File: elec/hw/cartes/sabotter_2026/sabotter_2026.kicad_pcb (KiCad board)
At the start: 4 copper layers, 65 x 100 mm, 139 parts, among them J1 22272021, J10 2-1445051-3, J11 22272051, J12 22272031, J13 3-794630-6, J17 22272061, J3 USB4120-03-C, J5 22272041, J6 3-794630-4, J9 3-794630-4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

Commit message: sabotter corrected after review
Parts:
- removed the R65 at (164.6, 81.8)
- removed the SW3 at (170.0, 79.2)
- added R27: 100k, cocotter_resistor:r0603_reflow, F.Cu at (113.0, 67.2)
- added R35: 100k, cocotter_resistor:r0603_reflow, F.Cu at (113.0, 65.5)
- added R36: 100k, cocotter_resistor:r0603_reflow, F.Cu at (113.0, 63.9)
- added R37: 0R, cocotter_resistor:r0603_reflow, F.Cu at (122.0, 93.8)
- D3: value 1N5819WS -> BZT52C3V0S; footprint cocotter_diodes:D_SOD-323 -> cocotter_diodes:SOD-323
- R1: value 22k 1% -> 100k
- R13, R14, R15, R2, R21, R24, R26, R30, R31, R32, R33, R34, R40, R42, R44, R46, R49, R51, R52, R55, R62, R63, R64, R68: value 91k 1% -> 100k
- moved D3 4.10 mm to (159.2, 22.5)
- moved R1 2.70 mm to (113.0, 62.2), turned to 180 degrees
- moved R2 1.00 mm to (161.5, 25.2)
- moved C3 1.00 mm to (161.5, 22.0)
- moved R3 1.00 mm to (163.5, 22.0)
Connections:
- net /interfaces/i2C_io_int_3v3 renamed /interfaces/irq_io_3v3
- D2 pad A: Net-(D1-K) -> Net-(D2-PadA)
- D2 pad C: Net-(D2-PadC) -> GND
- D3 pad 1: +3V3 -> /uc/esp32_vbatt_mon_3v1
- D3 pad 2: /uc/esp32_vbatt_mon_3v1 -> GND
- J18 pad 3: (no net) -> Net-(J18-NC)
- R1 pad 1: Net-(D2-PadC) -> Net-(D1-K)
- R1 pad 2: GND -> Net-(D2-PadA)
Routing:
- net /motors/ENCODER_A_MOT2_3V3: track 190.4 -> 90.4 mm
- net /motors/ENCODER_B_MOT0_3V3: track 147.7 -> 90.8 mm
- net /motors/ENCODER_B_MOT1_3V3: track 39.0 -> 92.4 mm
- net /motors/ENCODER_A_MOT0_3V3: track 119.6 -> 79.6 mm
- net /motors/DIR_MOT0_3V3: track 59.4 -> 89.0 mm
- net /motors/ENCODER_B_MOT2_3V3: track 111.1 -> 88.4 mm
- net /motors/irq0_3v3: track 68.2 -> 50.5 mm
- net /brake_mot_3v3: track 79.1 -> 63.3 mm
- net /interfaces/scl_3v3: track 147.1 -> 132.8 mm
- net /motors/DIR_MOT1_3V3: track 94.7 -> 107.1 mm
- net /uc/EN_ESP32_3v3: track 84.9 -> 74.9 mm
- net /interfaces/ctc_right_3v3: track 22.7 -> 15.2 mm
- net /interfaces/ctc_left_3v3: track 30.2 -> 23.2 mm
- net Net-(D2-PadA): track 0.00 -> 6.55 mm
- net +5V: track 188.8 -> 195.3 mm, vias 16 -> 17
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
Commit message: sabotter updated after review
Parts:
- added R38: 0R, cocotter_resistor:r0603_reflow, F.Cu at (161.5, 31.0)
- added R72: 0R, cocotter_resistor:r0603_reflow, F.Cu at (166.0, 33.8)
- added R73: 0R, cocotter_resistor:r0603_reflow, F.Cu at (146.5, 43.8)
- added R74: 0R, cocotter_resistor:r0603_reflow, F.Cu at (147.9, 43.8)
- added R75: 0R, cocotter_resistor:r0603_reflow, F.Cu at (134.2, 31.5)
- added R76: 0R, cocotter_resistor:r0603_reflow, F.Cu at (134.2, 32.9)
- R16, R17: value 390R 1% -> 0R
- R30, R33: value 100k -> 0R
- moved R29 37.3 mm to (160.5, 25.5), turned to 180 degrees
- moved R28 36.6 mm to (158.5, 33.8)
- moved R30 29.6 mm to (143.7, 43.8), turned to 90 degrees
- moved R33 28.2 mm to (145.1, 43.8)
- moved R2 2.02 mm to (163.5, 25.0)
- moved R31 1.72 mm to (160.0, 31.0), turned to -90 degrees
- moved TP6 1.00 mm to (116.5, 54.8)
- moved R32 0.75 mm to (166.6, 35.8)
- moved R34 0.75 mm to (166.6, 37.2)
- moved TP1 0.65 mm to (149.9, 44.8)
- moved C7 0.30 mm to (121.5, 69.7)
- moved C6 0.20 mm to (126.5, 61.2)
- moved J3 0.20 mm to (114.8, 44.0)
- moved TP3 0.18 mm to (133.1, 30.1)
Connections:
- J5 pad 1: /sensors/lidar_rx_3v3 -> Net-(J5-Pad1)
- J5 pad 2: /sensors/lidar_pwm_3v3 -> Net-(J5-Pad2)
- R30 pad 1: +3V3 -> /motors/ENCODER_A_MOT0_3V3
- R30 pad 2: /sensors/lidar_pwm_3v3 -> Net-(U3-IO11,RTC_GPIO11,GPIO11,TOUCH11,FSPID,FSPIIO5,SUBSPID)
- R33 pad 1: +3V3 -> /motors/ENCODER_B_MOT0_3V3
- R33 pad 2: /sensors/lidar_rx_3v3 -> Net-(U3-IO12,RTC_GPIO12,GPIO12,TOUCH12,FSPICLK,FSPIIO6,SUBSPICLK)
- U3 pad 19: /motors/ENCODER_A_MOT0_3V3 -> Net-(U3-IO11,RTC_GPIO11,GPIO11,TOUCH11,FSPID,FSPIIO5,SUBSPID)
- U3 pad 20: /motors/ENCODER_B_MOT0_3V3 -> Net-(U3-IO12,RTC_GPIO12,GPIO12,TOUCH12,FSPICLK,FSPIIO6,SUBSPICLK)
- U3 pad 21: /motors/ENCODER_B_MOT2_3V3 -> Net-(U3-IO13,RTC_GPIO13,GPIO13,TOUCH13,FSPIQ,FSPIIO7,SUBSPIQ)
- U3 pad 22: /motors/ENCODER_A_MOT2_3V3 -> Net-(U3-IO14,RTC_GPIO14,GPIO14,TOUCH14,FSPIWP,FSPIDQS,SUBSPIWP)
- U3 pad 8: /motors/ENCODER_B_MOT1_3V3 -> Net-(U3-IO15,RTC_GPIO15,GPIO15,U0RTS,XTAL_32K_P)
- U3 pad 9: /motors/ENCODER_A_MOT1_3V3 -> Net-(U3-IO16,RTC_GPIO16,GPIO16,U0CTS,XTAL_32K_N)
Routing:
- net /sensors/rx_from_r3d2_3v3: track 4.81 -> 42.1 mm
- net /sensors/lidar_rx_3v3: track 50.9 -> 14.4 mm
- net /sensors/tx_to_r3d2_3v3: track 3.85 -> 40.0 mm, vias 1 -> 3
- net /sensors/lidar_pwm_3v3: track 51.0 -> 23.2 mm
- net /motors/ENCODER_B_MOT0_3V3: track 90.8 -> 76.4 mm
- net +3V3: track 88.8 -> 84.5 mm, vias 27 -> 25
- net /motors/ENCODER_A_MOT0_3V3: track 79.6 -> 75.4 mm
- net /motors/ENCODER_A_MOT1_3V3: track 91.8 -> 88.0 mm
- net /motors/ENCODER_B_MOT1_3V3: track 92.4 -> 88.6 mm
- net /motors/ENCODER_A_MOT2_3V3: track 90.4 -> 86.6 mm
- net Net-(D1-K): track 106.5 -> 109.9 mm
- net /motors/ENCODER_B_MOT2_3V3: track 88.4 -> 85.1 mm
- net Net-(U3-IO12,RTC_GPIO12,GPIO12,TOUCH12,FSPICLK,FSPIIO6,SUBSPICLK): track 0.00 -> 2.76 mm
- net Net-(U3-IO11,RTC_GPIO11,GPIO11,TOUCH11,FSPID,FSPIIO5,SUBSPID): track 0.00 -> 2.72 mm
- net Net-(J5-Pad1): track 0.00 -> 2.59 mm
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
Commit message: jlcpcb part added
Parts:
- C6, C7: value 22µF 16V -> 22µF 25V
- J14, J15, J16: value ~ -> 1-188275-6
- J18, J4: value ~ -> 188275-4
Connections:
- J4 pad 3: (no net) -> unconnected-(J4-NC-Pad3)

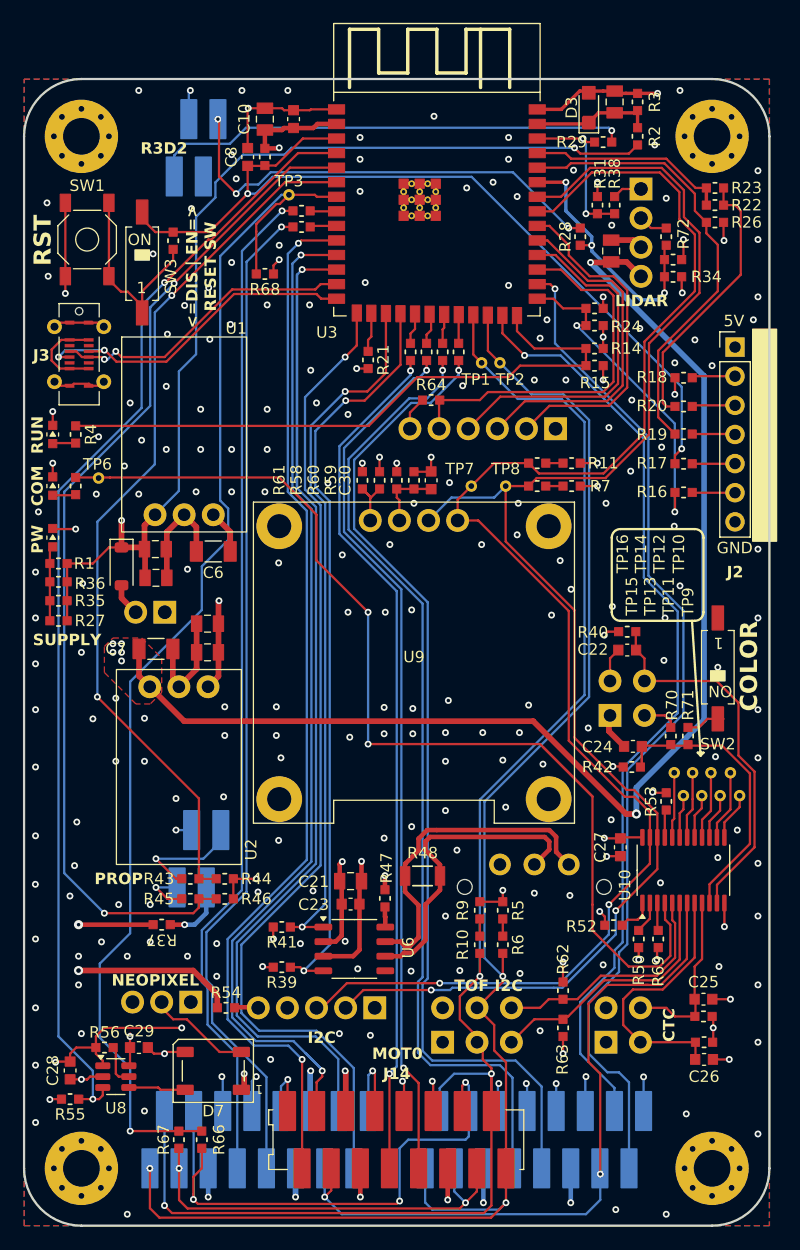
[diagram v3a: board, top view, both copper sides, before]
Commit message: oki78 footprint corrected
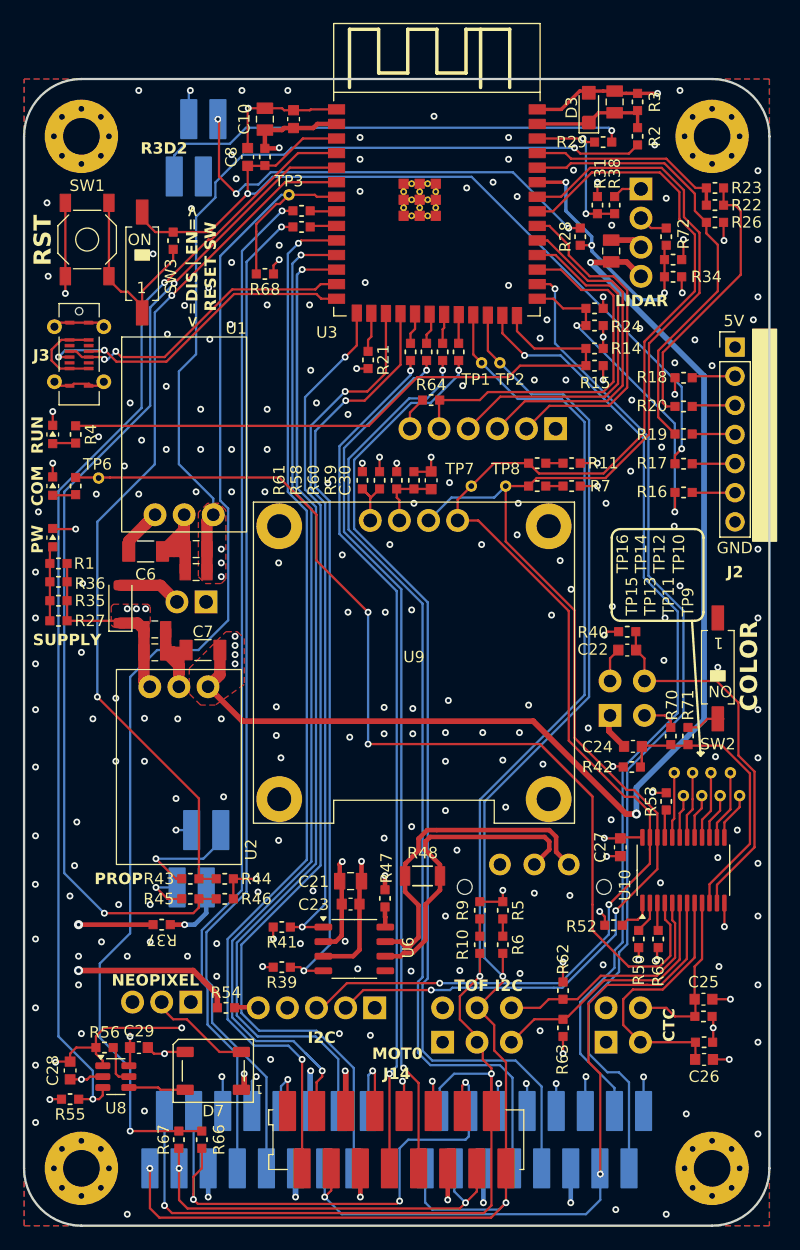
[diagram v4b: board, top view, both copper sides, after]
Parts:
- moved C6 5.90 mm to (120.6, 61.2), turned to 0 degrees
- moved C5 5.24 mm to (121.4, 70.0), turned to 0 degrees
- moved C2 5.02 mm to (121.4, 68.0), turned to 0 degrees
- moved C7 4.10 mm to (125.6, 69.8), turned to 180 degrees
- moved J1 3.71 mm to (124.6, 65.6)
- moved C1 3.55 mm to (125.0, 61.0), turned to 180 degrees
- moved C4 3.54 mm to (125.0, 63.0), turned to 180 degrees
- moved D1 3.30 mm to (118.4, 65.8), turned to 90 degrees
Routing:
- net Net-(D1-K): track 109.9 -> 92.6 mm, vias 3 -> 7
- net +5V: track 195.2 -> 190.4 mm, vias 17 -> 16
- net GND: track 156.4 -> 161.1 mm, vias 228 -> 227
- net +BATT: track 2.86 -> 5.53 mm
- net /motors/tof_irq_3v3: track 109.8 -> 111.9 mm
- net +3V3: track 84.5 -> 86.3 mm
- added copper zone on F.Cu, net Net-(D1-K)
- added copper zone on In2.Cu, net Net-(D1-K)

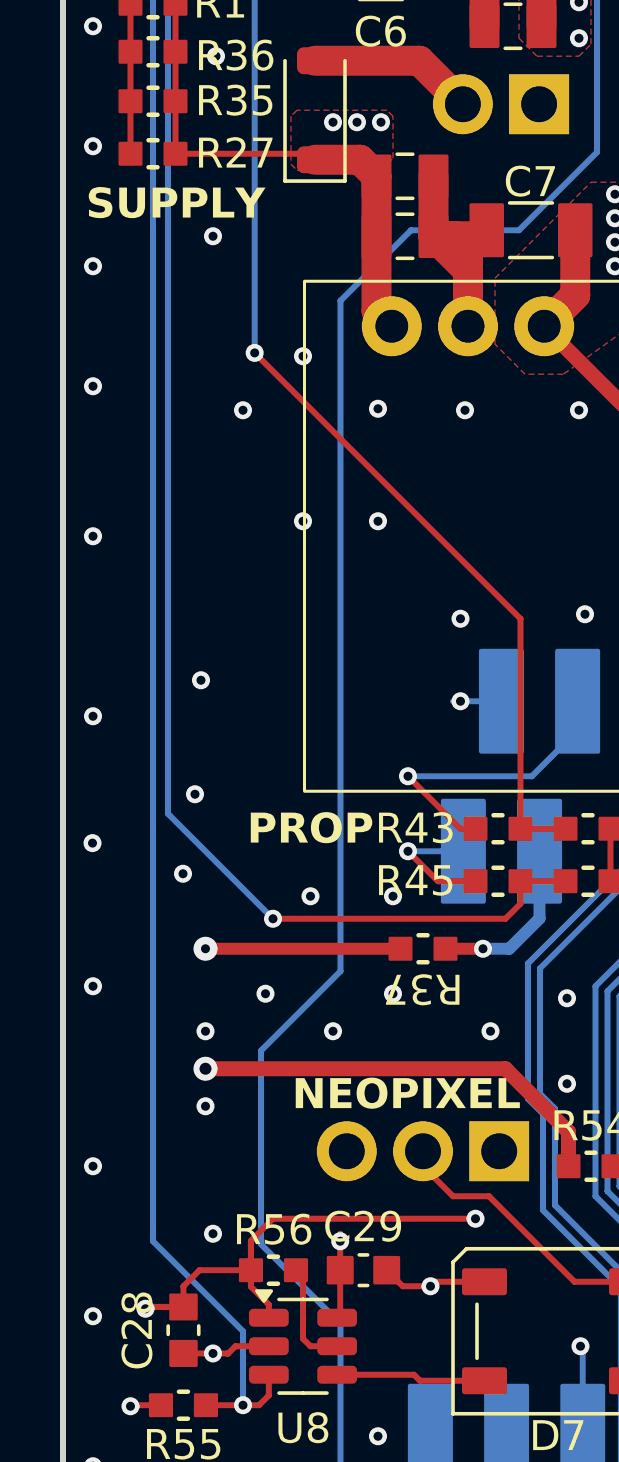
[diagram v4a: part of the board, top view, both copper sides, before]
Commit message: board name added
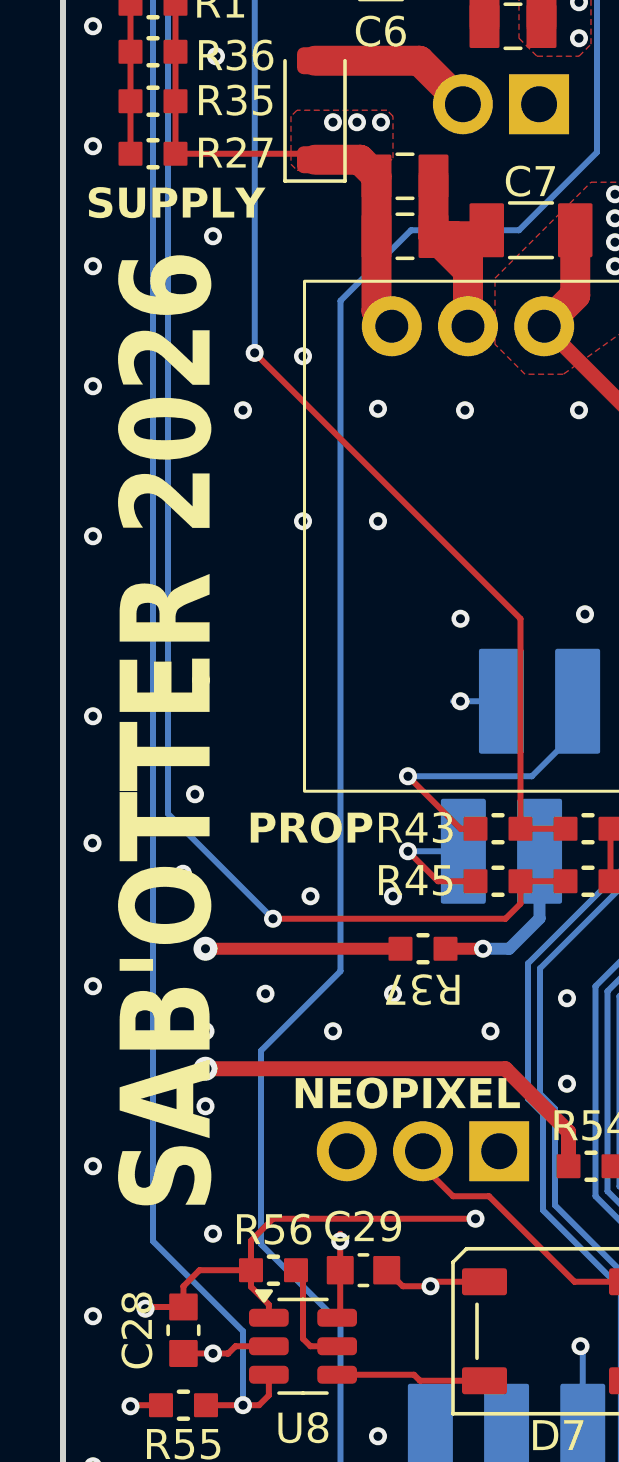
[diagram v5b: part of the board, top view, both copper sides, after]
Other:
- board text added: "SAB'OTTER 2026"
